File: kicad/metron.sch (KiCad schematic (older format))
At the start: 9 parts, among them J1 ftdi, J2 HCSR04, J3 OLED, SW1 SW_Push, U1 ATtiny84A-PU

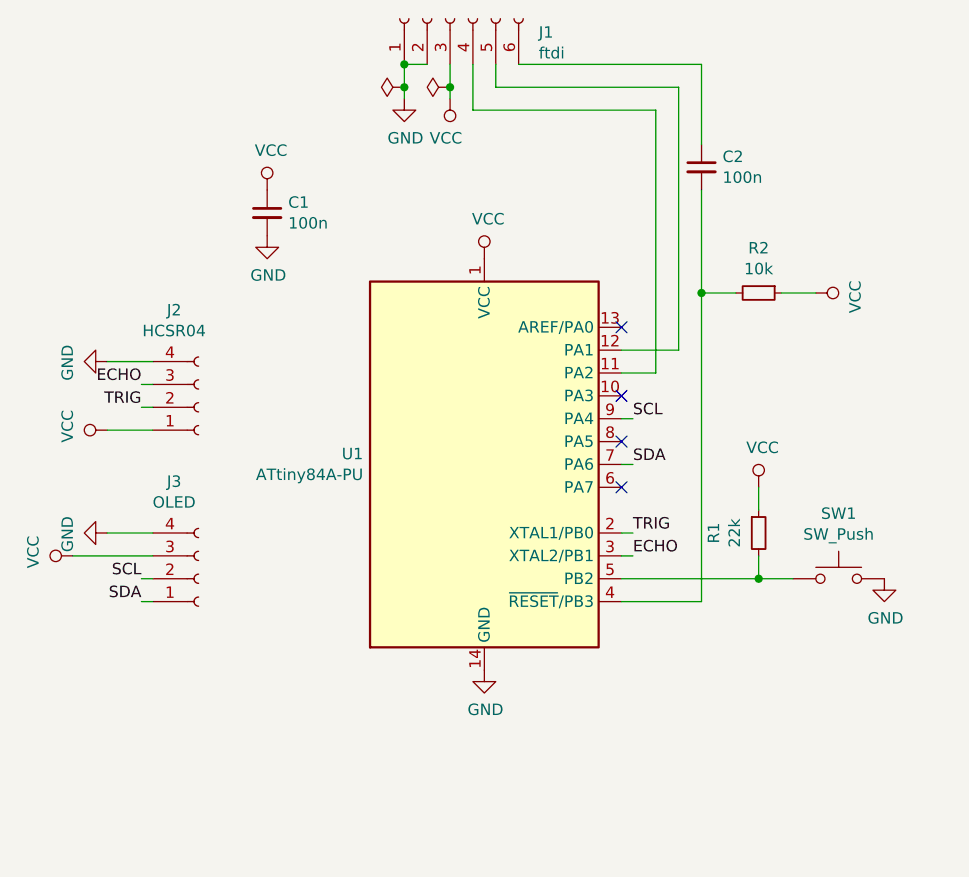
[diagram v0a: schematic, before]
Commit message: add battery
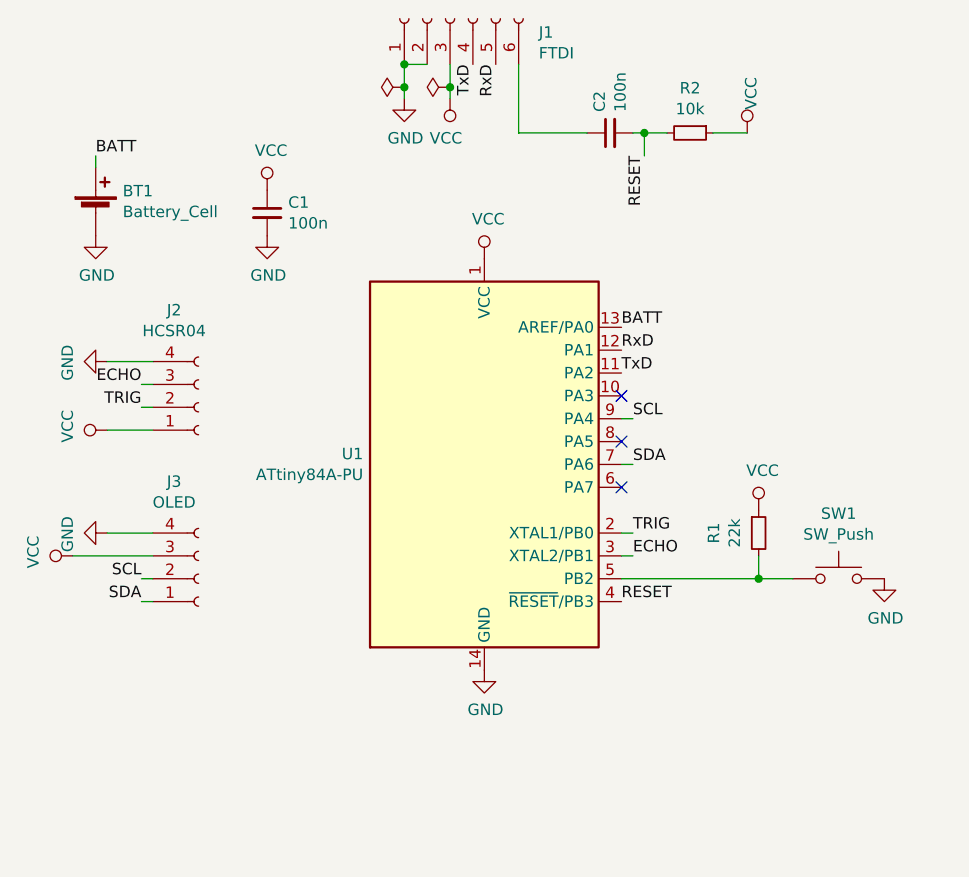
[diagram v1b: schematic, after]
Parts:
- added BT1: Battery_Cell, symbol Device:Battery_Cell
- J1: value ftdi -> FTDI
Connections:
- net GND: now also BT1.2 (-)
- net TxD: now reaches J1.4 (Pin_4), U1.11 (PA2)
- net RxD: now reaches J1.5 (Pin_5), U1.12 (PA1)
- net BATT: now reaches U1.13 (AREF/PA0)
- net BATT: now also BT1.1 (+)
- net RESET: now reaches C2.2, R2.2, U1.4 (~RESET~/PB3)
- no-connect marks 4 -> 3
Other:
- moved on the sheet: C2, R2
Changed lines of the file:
@@
 EESchema Schematic File Version 4
+LIBS:metron-cache
 EELAYER 26 0
 EELAYER END
@@
 P 4900 1150
 F 0 "J1" V 4840 762 50  0000 R CNN
-F 1 "ftdi" V 4749 762 50  0000 R CNN
+F 1 "FTDI" V 4749 762 50  0000 R CNN
 F 2 "Connector_PinHeader_2.54mm:PinHeader_1x06_P2.54mm_Vertical" H 4900 1150 50  0001 C CNN
 F 3 "~" H 4900 1150 50  0001 C CNN
@@
 Wire Wire Line
 	4900 1450 4900 1350
-Wire Wire Line
-	5650 2600 5900 2600
-Wire Wire Line
-	5900 2600 5900 1450
-Wire Wire Line
-	5900 1450 5100 1450
-Wire Wire Line
-	5100 1450 5100 1350
-Wire Wire Line
-	5650 2700 5800 2700
-Wire Wire Line
-	5800 2700 5800 1550
-Wire Wire Line
-	5800 1550 5000 1550
-Wire Wire Line
-	5000 1550 5000 1350
-Wire Wire Line
-	5200 1350 6000 1350
-Wire Wire Line
-	6000 1350 6000 1700
-$Comp
-L Device:C_Small C2
-U 1 1 5CFE4F03
-P 6000 1800
-F 0 "C2" H 6092 1846 50  0000 L CNN
-F 1 "100n" H 6092 1755 50  0000 L CNN
-F 2 "Capacitor_THT:C_Disc_D6.0mm_W2.5mm_P5.00mm" H 6000 1800 50  0001 C CNN
-F 3 "~" H 6000 1800 50  0001 C CNN
-	1    6000 1800
-	1    0    0    -1
-$EndComp
 $Comp
 L Device:C_Small C1
@@
 L Device:R_Small R2
 U 1 1 5CFE5177
-P 6250 2350
-F 0 "R2" V 6054 2350 50  0000 C CNN
-F 1 "10k" V 6145 2350 50  0000 C CNN
-F 2 "Resistor_THT:R_Axial_DIN0207_L6.3mm_D2.5mm_P10.16mm_Horizontal" H 6250 2350 50  0001 C CNN
-F 3 "~" H 6250 2350 50  0001 C CNN
-	1    6250 2350
+P 5950 1650
+F 0 "R2" V 5754 1650 50  0000 C CNN
+F 1 "10k" V 5845 1650 50  0000 C CNN
+F 2 "Resistor_THT:R_Axial_DIN0207_L6.3mm_D2.5mm_P10.16mm_Horizontal" H 5950 1650 50  0001 C CNN
+F 3 "~" H 5950 1650 50  0001 C CNN
+	1    5950 1650
 	0    1    1    0
 $EndComp
 Wire Wire Line
-	6350 2350 6500 2350
+	6050 1650 6200 1650
 $Comp
 L power:VCC #PWR08
 U 1 1 5CFE53CC
-P 6500 2350
-F 0 "#PWR08" H 6500 2200 50  0001 C CNN
-F 1 "VCC" H 6517 2523 50  0000 C CNN
-F 2 "" H 6500 2350 50  0001 C CNN
-F 3 "" H 6500 2350 50  0001 C CNN
-	1    6500 2350
-	0    1    1    0
+P 6200 1650
+F 0 "#PWR08" H 6200 1500 50  0001 C CNN
+F 1 "VCC" V 6217 1823 50  0000 C CNN
+F 2 "" H 6200 1650 50  0001 C CNN
+F 3 "" H 6200 1650 50  0001 C CNN
+	1    6200 1650
+	1    0    0    -1
 $EndComp
 $Comp
@@
 $EndComp
 Wire Wire Line
-	5650 3700 6000 3700
-Wire Wire Line
-	6000 3700 6000 2350
-Wire Wire Line
-	6000 2350 6150 2350
-Connection ~ 6000 2350
-Wire Wire Line
-	6000 2350 6000 1900
-Wire Wire Line
 	6250 3600 6250 3500
 Connection ~ 6250 3600
@@
 L power:VCC #PWR0103
 U 1 1 5E779F5A
-P 6250 3200
-F 0 "#PWR0103" H 6250 3050 50  0001 C CNN
-F 1 "VCC" H 6267 3373 50  0000 C CNN
-F 2 "" H 6250 3200 50  0001 C CNN
-F 3 "" H 6250 3200 50  0001 C CNN
-	1    6250 3200
-	1    0    0    -1
-$EndComp
-Wire Wire Line
-	6250 3200 6250 3300
+P 6250 3300
+F 0 "#PWR0103" H 6250 3150 50  0001 C CNN
+F 1 "VCC" H 6267 3473 50  0000 C CNN
+F 2 "" H 6250 3300 50  0001 C CNN
+F 3 "" H 6250 3300 50  0001 C CNN
+	1    6250 3300
+	1    0    0    -1
+$EndComp
 Wire Wire Line
 	3600 2750 3550 2750
@@
 Text Label 5700 2900 0    50   ~ 0
 SCL
-NoConn ~ 5650 2500
 NoConn ~ 5650 2800
 NoConn ~ 5650 3000
@@
 Wire Wire Line
 	5650 3600 6250 3600
+$Comp
+L Device:Battery_Cell BT1
+U 1 1 5E787B9E
+P 3350 2000
+F 0 "BT1" H 3468 2096 50  0000 L CNN
+F 1 "Battery_Cell" H 3468 2005 50  0000 L CNN
+F 2 "" V 3350 2060 50  0001 C CNN
+F 3 "~" V 3350 2060 50  0001 C CNN
+	1    3350 2000
+	1    0    0    -1
+$EndComp
+$Comp
+L power:GND #PWR011
+U 1 1 5E787BE8
+P 3350 2100
+F 0 "#PWR011" H 3350 1850 50  0001 C CNN
+F 1 "GND" H 3355 1927 50  0000 C CNN
+F 2 "" H 3350 2100 50  0001 C CNN
+F 3 "" H 3350 2100 50  0001 C CNN
+	1    3350 2100
+	1    0    0    -1
+$EndComp
+Wire Wire Line
+	3350 1800 3350 1750
+Text Label 3350 1750 0    50   ~ 0
+BATT
+Text Label 5650 2500 0    50   ~ 0
+BATT
+$Comp
+L Device:C_Small C2
+U 1 1 5CFE4F03
+P 5600 1650
+F 0 "C2" H 5692 1696 50  0000 L CNN
+F 1 "100n" H 5692 1605 50  0000 L CNN
+F 2 "Capacitor_THT:C_Disc_D6.0mm_W2.5mm_P5.00mm" H 5600 1650 50  0001 C CNN
+F 3 "~" H 5600 1650 50  0001 C CNN
+	1    5600 1650
+	0    -1   -1   0
+$EndComp
+Wire Wire Line
+	5850 1650 5750 1650
+Text Label 5650 3700 0    50   ~ 0
+RESET
+Wire Wire Line
+	5750 1650 5750 1750
+Connection ~ 5750 1650
+Wire Wire Line
+	5750 1650 5700 1650
+Text Label 5750 1750 3    50   ~ 0
+RESET
+Text Label 5100 1350 3    50   ~ 0
+RxD
+Text Label 5650 2600 0    50   ~ 0
+RxD
+Text Label 5650 2700 0    50   ~ 0
+TxD
+Text Label 5000 1350 3    50   ~ 0
+TxD
+Wire Wire Line
+	5200 1350 5200 1650
+Wire Wire Line
+	5200 1650 5500 1650
 $EndSCHEMATC

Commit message: update schematic
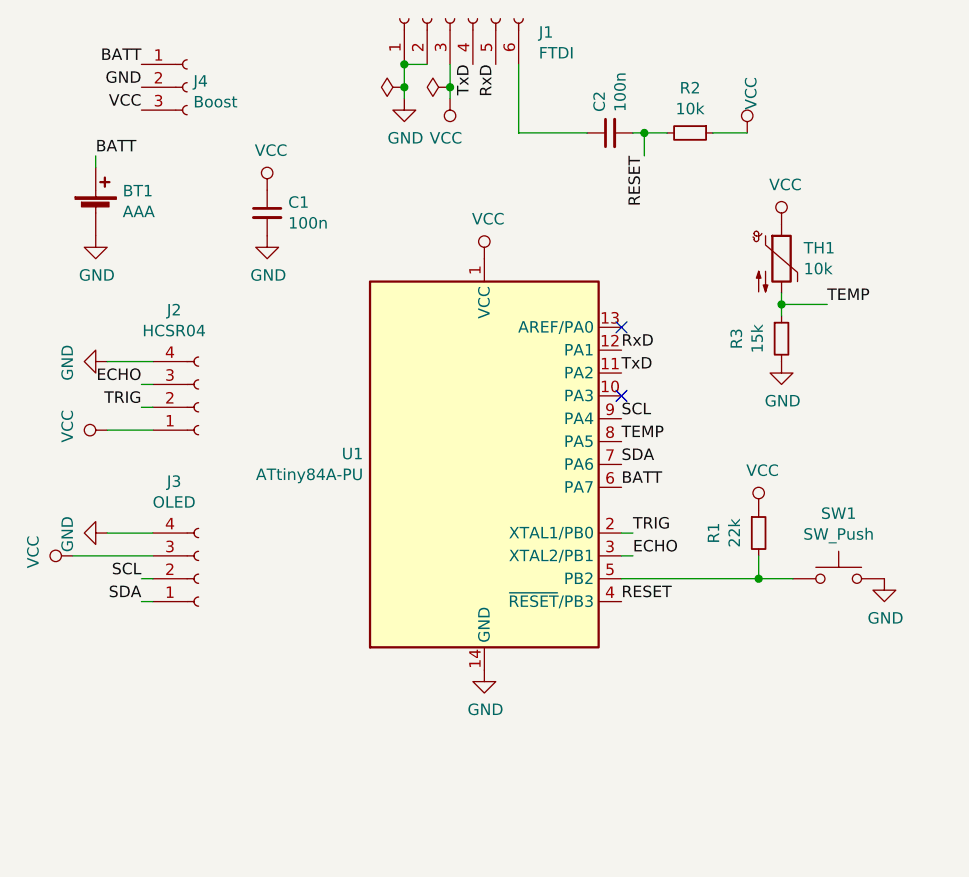
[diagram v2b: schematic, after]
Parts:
- added J4: Boost, symbol Connector:Conn_01x03_Female
- added R3: 15k, Resistor_THT:R_Axial_DIN0207_L6.3mm_D2.5mm_P10.16mm_Horizontal, symbol Device:R_Small
- added TH1: 10k, symbol Device:Thermistor_NTC
- BT1: value Battery_Cell -> AAA
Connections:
- net BATT: now also U1.6 (PA7), J4.1 (Pin_1); no longer U1.13 (AREF/PA0)
- net GND: now also J4.2 (Pin_2), R3.2
- net VCC: now also J4.3 (Pin_3), TH1.1
- net TEMP: now reaches U1.8 (PA5)
- net TEMP: now also R3.1, TH1.2
- no-connect marks 3 -> 2
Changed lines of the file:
@@
 Text Label 3550 3700 2    50   ~ 0
 SDA
-Wire Wire Line
-	5650 3100 5700 3100
-Wire Wire Line
-	5650 2900 5700 2900
-Text Label 5700 3100 0    50   ~ 0
+Text Label 5650 3100 0    50   ~ 0
 SDA
-Text Label 5700 2900 0    50   ~ 0
+Text Label 5650 2900 0    50   ~ 0
 SCL
 NoConn ~ 5650 2800
-NoConn ~ 5650 3000
-NoConn ~ 5650 3200
 Wire Wire Line
 	5650 3600 6250 3600
@@
 P 3350 2000
 F 0 "BT1" H 3468 2096 50  0000 L CNN
-F 1 "Battery_Cell" H 3468 2005 50  0000 L CNN
+F 1 "AAA" H 3468 2005 50  0000 L CNN
 F 2 "" V 3350 2060 50  0001 C CNN
 F 3 "~" V 3350 2060 50  0001 C CNN
@@
 	3350 1800 3350 1750
 Text Label 3350 1750 0    50   ~ 0
-BATT
-Text Label 5650 2500 0    50   ~ 0
 BATT
 $Comp
@@
 Wire Wire Line
 	5200 1650 5500 1650
+$Comp
+L Connector:Conn_01x03_Female J4
+U 1 1 5E79ED1F
+P 3750 1450
+F 0 "J4" H 3777 1476 50  0000 L CNN
+F 1 "Boost" H 3777 1385 50  0000 L CNN
+F 2 "" H 3750 1450 50  0001 C CNN
+F 3 "~" H 3750 1450 50  0001 C CNN
+	1    3750 1450
+	1    0    0    -1
+$EndComp
+Text Label 3550 1350 2    50   ~ 0
+BATT
+Text Label 3550 1450 2    50   ~ 0
+GND
+Text Label 3550 1550 2    50   ~ 0
+VCC
+Text Label 5650 3200 0    50   ~ 0
+BATT
+NoConn ~ 5650 2500
+Text Label 5650 3000 0    50   ~ 0
+TEMP
+$Comp
+L Device:Thermistor_NTC TH1
+U 1 1 5F2281A5
+P 6350 2200
+F 0 "TH1" H 6447 2246 50  0000 L CNN
+F 1 "10k" H 6447 2155 50  0000 L CNN
+F 2 "" H 6350 2250 50  0001 C CNN
+F 3 "~" H 6350 2250 50  0001 C CNN
+	1    6350 2200
+	1    0    0    -1
+$EndComp
+$Comp
+L Device:R_Small R3
+U 1 1 5F2281FD
+P 6350 2550
+F 0 "R3" V 6154 2550 50  0000 C CNN
+F 1 "15k" V 6245 2550 50  0000 C CNN
+F 2 "Resistor_THT:R_Axial_DIN0207_L6.3mm_D2.5mm_P10.16mm_Horizontal" H 6350 2550 50  0001 C CNN
+F 3 "~" H 6350 2550 50  0001 C CNN
+	1    6350 2550
+	1    0    0    -1
+$EndComp
+Wire Wire Line
+	6350 2350 6350 2400
+Wire Wire Line
+	6350 2400 6550 2400
+Connection ~ 6350 2400
+Wire Wire Line
+	6350 2400 6350 2450
+Text Label 6550 2400 0    50   ~ 0
+TEMP
+$Comp
+L power:VCC #PWR0104
+U 1 1 5F2288E4
+P 6350 2050
+F 0 "#PWR0104" H 6350 1900 50  0001 C CNN
+F 1 "VCC" H 6367 2223 50  0000 C CNN
+F 2 "" H 6350 2050 50  0001 C CNN
+F 3 "" H 6350 2050 50  0001 C CNN
+	1    6350 2050
+	1    0    0    -1
+$EndComp
+$Comp
+L power:GND #PWR0105
+U 1 1 5F228916
+P 6350 2650
+F 0 "#PWR0105" H 6350 2400 50  0001 C CNN
+F 1 "GND" H 6355 2477 50  0000 C CNN
+F 2 "" H 6350 2650 50  0001 C CNN
+F 3 "" H 6350 2650 50  0001 C CNN
+	1    6350 2650
+	1    0    0    -1
+$EndComp
 $EndSCHEMATC

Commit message: update schematic with device-power switch
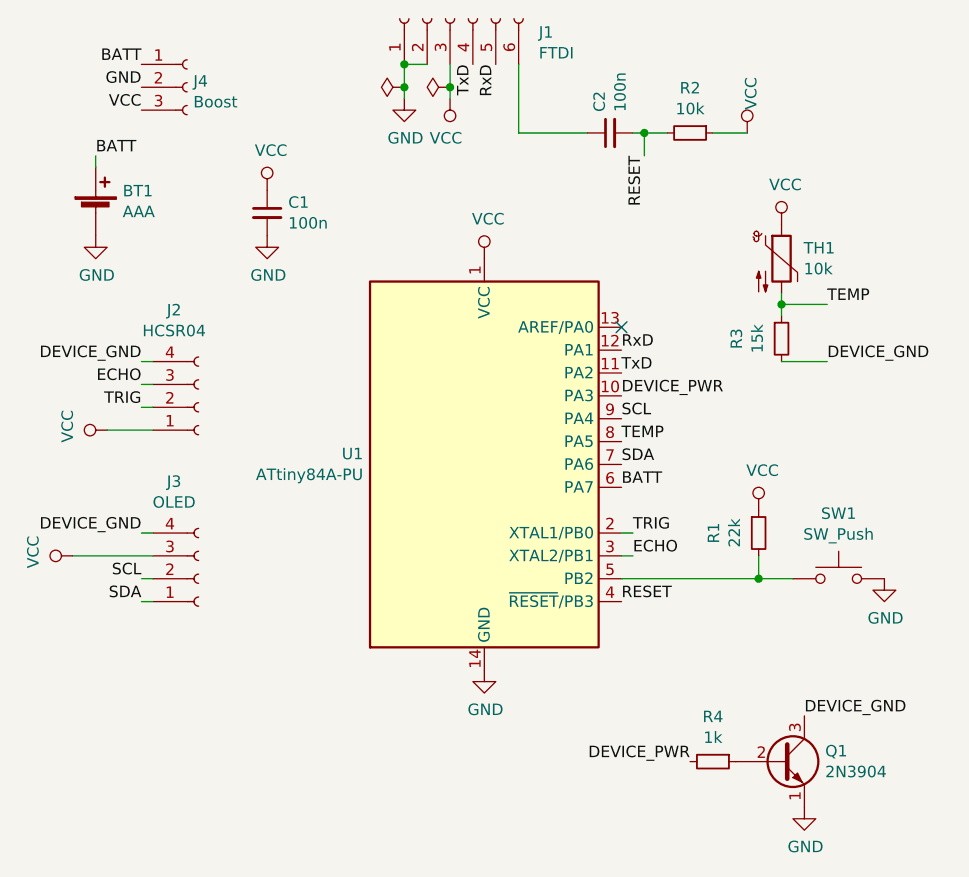
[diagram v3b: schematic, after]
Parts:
- added Q1: 2N3904, Package_TO_SOT_THT:TO-92_Inline, symbol Transistor_BJT:2N3904
- added R4: 1k, Resistor_THT:R_Axial_DIN0207_L6.3mm_D2.5mm_P10.16mm_Horizontal, symbol Device:R_Small
- TH1: footprint (none) -> Resistor_THT:R_Axial_DIN0207_L6.3mm_D2.5mm_P10.16mm_Horizontal
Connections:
- net GND: now also Q1.1 (E); no longer J2.4 (Pin_4), J3.4 (Pin_4), R3.2
- net DEVICE_PWR: now reaches U1.10 (PA3)
- net DEVICE_PWR: now also R4.2
- new net: Q1.2 (B), R4.1
- new net DEVICE_GND: J2.4 (Pin_4), J3.4 (Pin_4), Q1.3 (C), R3.2
- no-connect marks 2 -> 1
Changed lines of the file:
@@
-$EndComp
-$Comp
-L power:GND #PWR0101
-U 1 1 5E777A83
-P 3400 2650
-F 0 "#PWR0101" H 3400 2400 50  0001 C CNN
-F 1 "GND" H 3405 2477 50  0000 C CNN
-F 2 "" H 3400 2650 50  0001 C CNN
-F 3 "" H 3400 2650 50  0001 C CNN
-	1    3400 2650
-	0    1    1    0
 $EndComp
 $Comp
@@
 $EndComp
 Wire Wire Line
-	3400 2650 3600 2650
-Wire Wire Line
 	3400 2950 3600 2950
 $Comp
@@
 $EndComp
 $Comp
-L power:GND #PWR010
-U 1 1 5E77BE90
-P 3400 3400
-F 0 "#PWR010" H 3400 3150 50  0001 C CNN
-F 1 "GND" H 3405 3227 50  0000 C CNN
-F 2 "" H 3400 3400 50  0001 C CNN
-F 3 "" H 3400 3400 50  0001 C CNN
-	1    3400 3400
-	0    1    1    0
-$EndComp
-$Comp
 L power:VCC #PWR07
 U 1 1 5E77BE96
@@
 $EndComp
 Wire Wire Line
-	3400 3400 3600 3400
-Wire Wire Line
 	3250 3500 3600 3500
 Wire Wire Line
@@
 Text Label 5650 2900 0    50   ~ 0
 SCL
-NoConn ~ 5650 2800
 Wire Wire Line
 	5650 3600 6250 3600
@@
 F 0 "TH1" H 6447 2246 50  0000 L CNN
 F 1 "10k" H 6447 2155 50  0000 L CNN
-F 2 "" H 6350 2250 50  0001 C CNN
+F 2 "Resistor_THT:R_Axial_DIN0207_L6.3mm_D2.5mm_P10.16mm_Horizontal" H 6350 2250 50  0001 C CNN
 F 3 "~" H 6350 2250 50  0001 C CNN
 	1    6350 2200
@@
 $EndComp
 $Comp
-L power:GND #PWR0105
-U 1 1 5F228916
-P 6350 2650
-F 0 "#PWR0105" H 6350 2400 50  0001 C CNN
-F 1 "GND" H 6355 2477 50  0000 C CNN
-F 2 "" H 6350 2650 50  0001 C CNN
-F 3 "" H 6350 2650 50  0001 C CNN
-	1    6350 2650
-	1    0    0    -1
-$EndComp
+L Transistor_BJT:2N3904 Q1
+U 1 1 5F4FBD5A
+P 6350 4400
+F 0 "Q1" H 6541 4446 50  0000 L CNN
+F 1 "2N3904" H 6541 4355 50  0000 L CNN
+F 2 "Package_TO_SOT_THT:TO-92_Inline" H 6550 4325 50  0001 L CIN
+F 3 "https://www.fairchildsemi.com/datasheets/2N/2N3904.pdf" H 6350 4400 50  0001 L CNN
+	1    6350 4400
+	1    0    0    -1
+$EndComp
+$Comp
+L Device:R_Small R4
+U 1 1 5F4FBEDF
+P 6050 4400
+F 0 "R4" V 5854 4400 50  0000 C CNN
+F 1 "1k" V 5945 4400 50  0000 C CNN
+F 2 "Resistor_THT:R_Axial_DIN0207_L6.3mm_D2.5mm_P10.16mm_Horizontal" H 6050 4400 50  0001 C CNN
+F 3 "~" H 6050 4400 50  0001 C CNN
+	1    6050 4400
+	0    1    1    0
+$EndComp
+$Comp
+L power:GND #PWR010
+U 1 1 5F4FBF89
+P 6450 4600
+F 0 "#PWR010" H 6450 4350 50  0001 C CNN
+F 1 "GND" H 6455 4427 50  0000 C CNN
+F 2 "" H 6450 4600 50  0001 C CNN
+F 3 "" H 6450 4600 50  0001 C CNN
+	1    6450 4600
+	1    0    0    -1
+$EndComp
+Text Label 6450 4200 0    50   ~ 0
+DEVICE_GND
+Text Label 5650 2800 0    50   ~ 0
+DEVICE_PWR
+Text Label 6550 2650 0    50   ~ 0
+DEVICE_GND
+Wire Wire Line
+	6350 2650 6550 2650
+Text Label 3550 2650 2    50   ~ 0
+DEVICE_GND
+Wire Wire Line
+	3600 2650 3550 2650
+Wire Wire Line
+	3600 3400 3550 3400
+Text Label 3550 3400 2    50   ~ 0
+DEVICE_GND
+Text Label 5950 4400 2    50   ~ 0
+DEVICE_PWR
 $EndSCHEMATC
